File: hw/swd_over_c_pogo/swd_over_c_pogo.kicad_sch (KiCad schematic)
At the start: 7 parts, among them J1 Conn_01x06

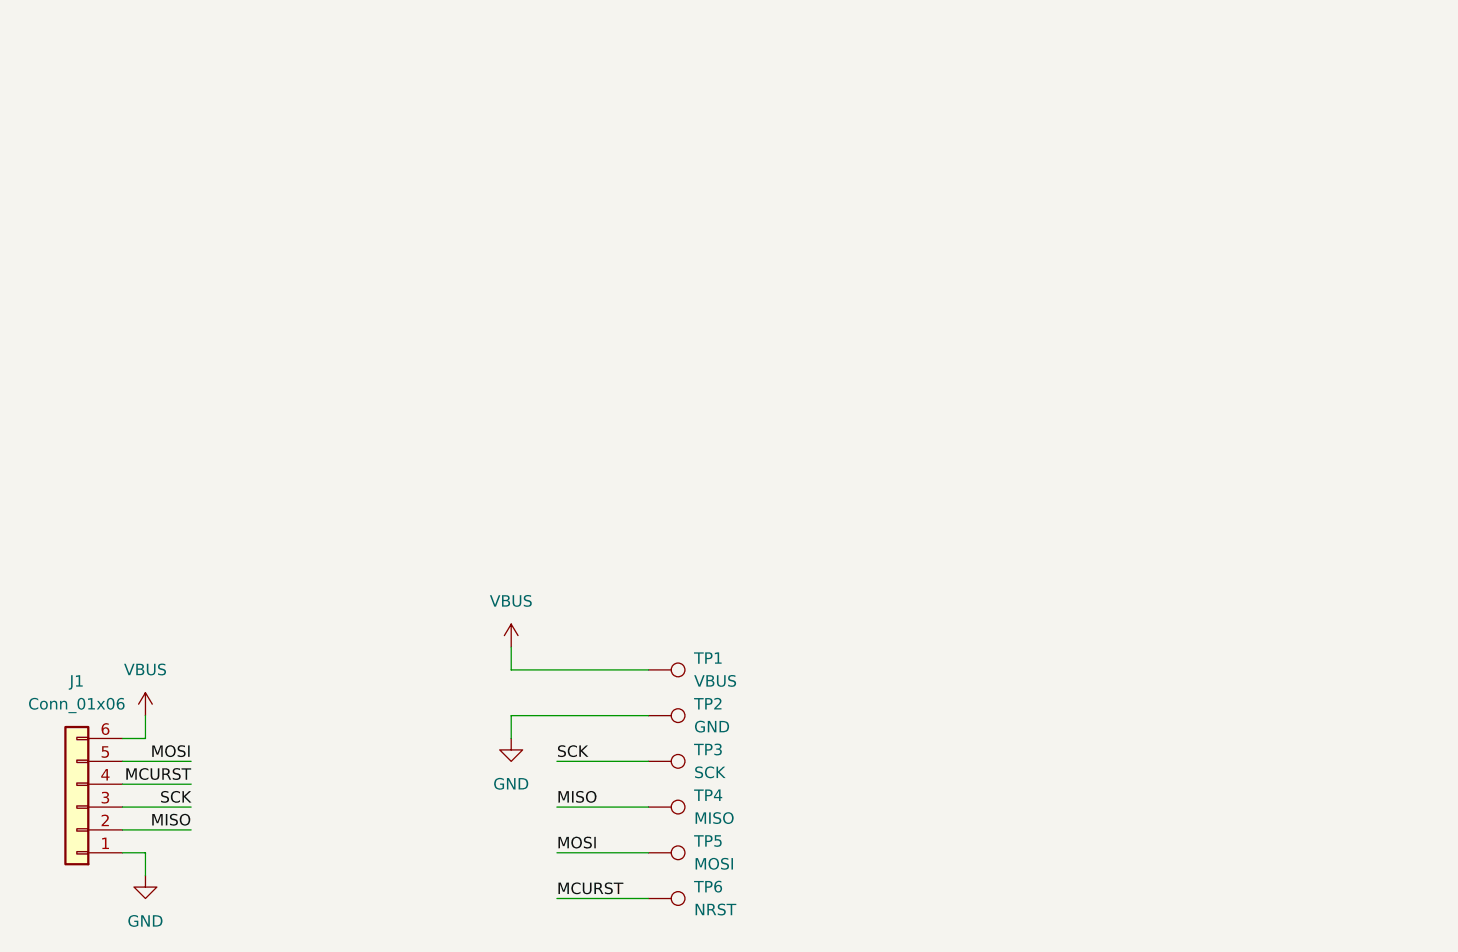
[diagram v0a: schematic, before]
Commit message: Updated swd over c to v1.1 (and programmer)
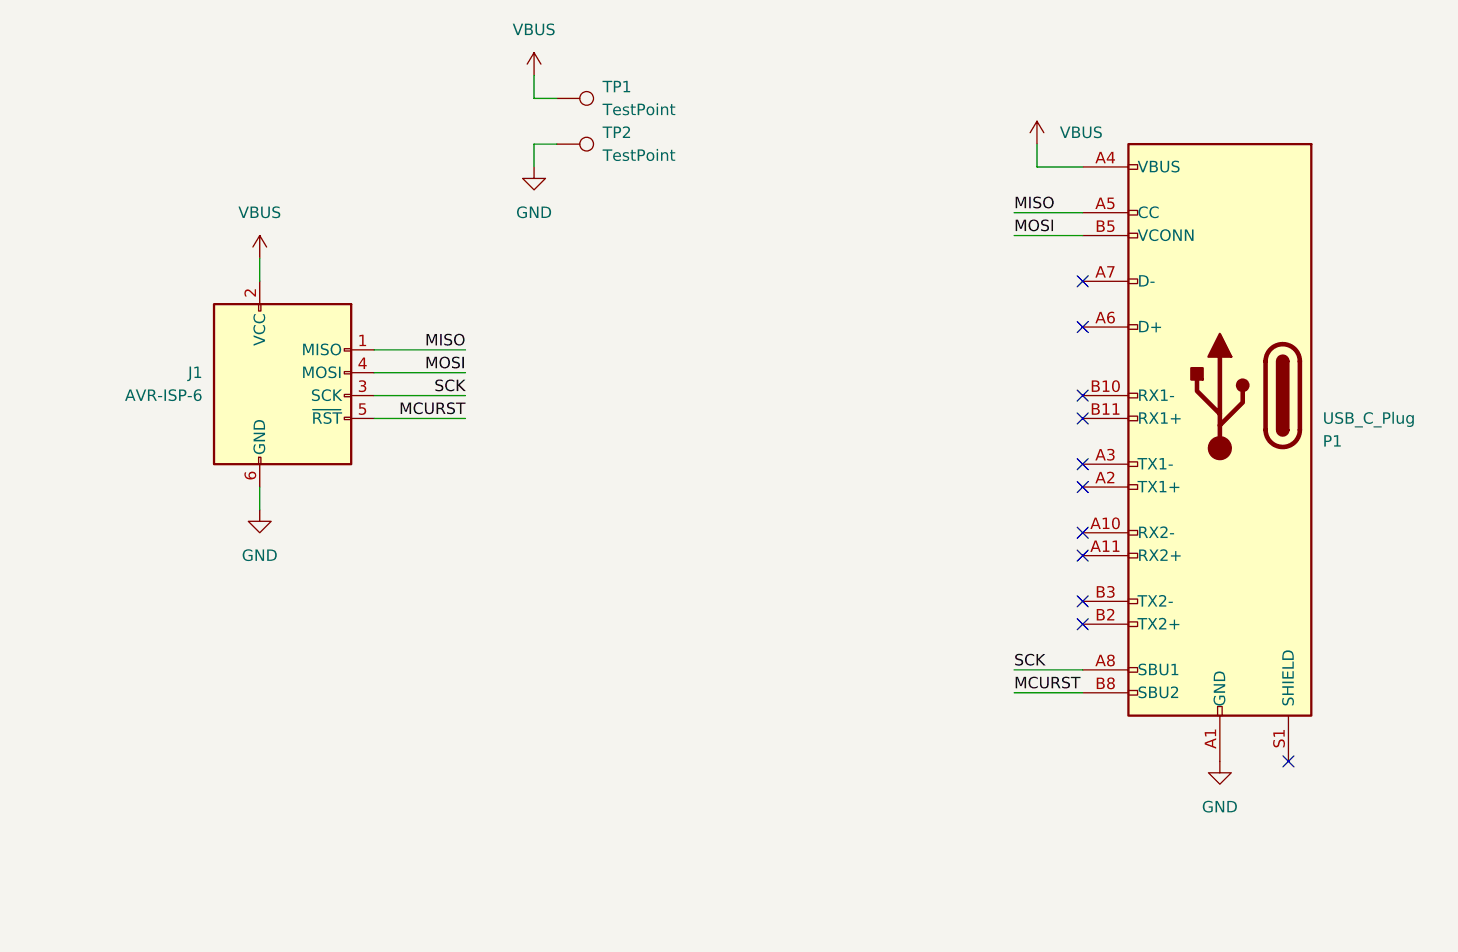
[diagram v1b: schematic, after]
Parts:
- removed J1: Conn_01x06, Connector_PinHeader_1.27mm:PinHeader_1x06_P1.27mm_Horizontal, symbol Connector_Generic:Conn_01x06
- removed TP3: SCK, alvarop:0906-3-15-20-75-14-11-0, symbol Connector:TestPoint
- removed TP4: MISO, alvarop:0906-3-15-20-75-14-11-0, symbol Connector:TestPoint
- removed TP5: MOSI, alvarop:0906-3-15-20-75-14-11-0, symbol Connector:TestPoint
- removed TP6: NRST, alvarop:0906-3-15-20-75-14-11-0, symbol Connector:TestPoint
- added J1: AVR-ISP-6, Connector_IDC:IDC-Header_2x03_P2.54mm_Vertical, symbol Connector:AVR-ISP-6
- added P1: USB_C_Plug, alvarop:USB4151-GF-C, symbol Connector:USB_C_Plug
- TP1: value VBUS -> TestPoint; footprint alvarop:0906-3-15-20-75-14-11-0 -> TestPoint:TestPoint_Pad_D2.5mm
- TP2: value GND -> TestPoint; footprint alvarop:0906-3-15-20-75-14-11-0 -> TestPoint:TestPoint_Pad_D2.5mm
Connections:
- net GND: now also J1.6 (GND), P1.A1 (GND), P1.A12 (GND), P1.B1 (GND), P1.B12 (GND)
- net MCURST: now also J1.5 (~{RST}), P1.B8 (SBU2)
- net MISO: now also J1.1 (MISO), P1.A5 (CC)
- net MOSI: now also J1.4 (MOSI), P1.B5 (VCONN)
- net SCK: now also J1.3 (SCK), P1.A8 (SBU1)
- net VBUS: now also J1.2 (VCC), P1.A4 (VBUS), P1.A9 (VBUS), P1.B4 (VBUS), P1.B9 (VBUS)
- no-connect marks 0 -> 11

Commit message: Minor bom updates
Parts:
- J1: MPN (none) -> 30306-6002HB
- P1: MPN (none) -> USB4151-GF-C
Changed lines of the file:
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@@
+      (effects (font (size 1.27 1.27)) hide)
+    )
+    (property "MPN" " USB4151-GF-C" (id 4) (at 147.32 121.92 0)
       (effects (font (size 1.27 1.27)) hide)
     )
@@
       (effects (font (size 1.27 1.27)) hide)
     )
+    (property "MPN" "30306-6002HB" (id 4) (at 43.18 121.92 0)
+      (effects (font (size 1.27 1.27)) hide)
+    )

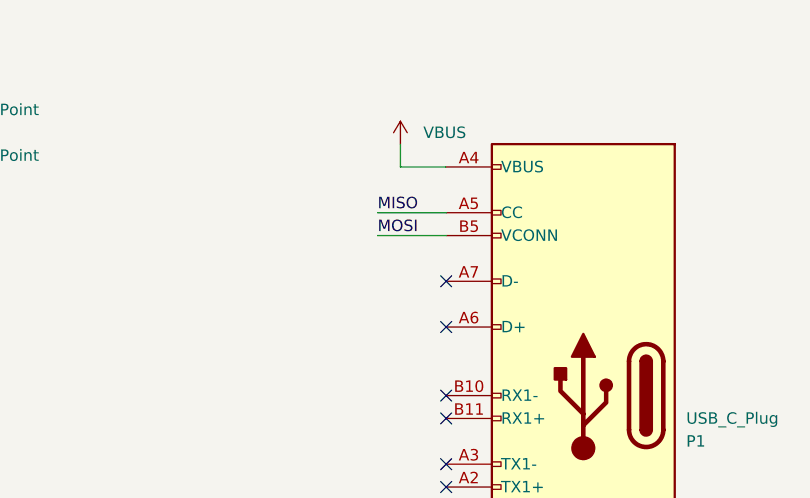
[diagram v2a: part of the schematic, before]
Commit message: Fixed MISO/MOSI swap and added BOM to swd2usbc
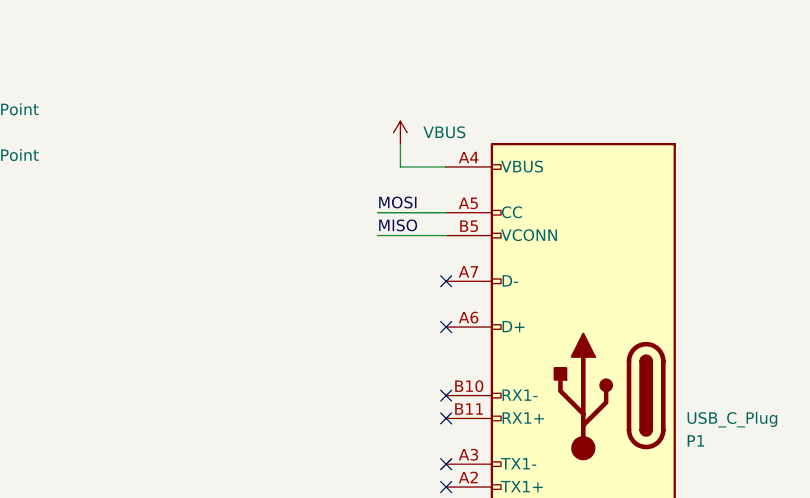
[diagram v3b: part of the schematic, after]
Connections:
- net MISO: now also P1.B5 (VCONN); no longer P1.A5 (CC)
- net MOSI: now also P1.A5 (CC); no longer P1.B5 (VCONN)
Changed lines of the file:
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@@
   (title_block
     (title "Debugotron - SWD to USBC Programmer")
-    (date "2022-02-06")
-    (rev "1.1")
+    (date "2022-03-04")
+    (rev "1.2")
     (company "Quesadillon LLC")
   )
@@
     (effects (font (size 1.27 1.27)) (justify right bottom))
   )
-  (label "MISO" (at 124.46 101.6 0)
+  (label "MISO" (at 124.46 104.14 0)
     (effects (font (size 1.27 1.27)) (justify left bottom))
   )
@@
     (effects (font (size 1.27 1.27)) (justify right bottom))
   )
-  (label "MOSI" (at 124.46 104.14 0)
+  (label "MOSI" (at 124.46 101.6 0)
     (effects (font (size 1.27 1.27)) (justify left bottom))
   )
